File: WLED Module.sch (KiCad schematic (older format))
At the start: 16 parts, among them IC1 SN74AHCT125D, J1 Conn_01x06_Male, J2 1725669, J3 POWER_JACKPTH_BREAD, Q1 SS8050-G, Q2 SS8050-G, U1 ESP32-WROOM-32D, U2 AMS1117-3.3

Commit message: Various revisions:
Input lines on IC1 tied to VCC.
Input power connector changed to JST VH type.
Decoupling capacitors changed to 0.1uf.

Initial Gerber & other fab files generated.
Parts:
- removed J3: POWER_JACKPTH_BREAD, Connectors:POWER_JACK_PTH_BREAD, symbol SparkFun-Connectors:POWER_JACKPTH_BREAD
- added C6: 0.1uF 50V, Capacitor_SMD:C_0805_2012Metric_Pad1.15x1.40mm_HandSolder, symbol Device:C
- added F1: 10A, Fuse:Fuseholder_Blade_Mini_Keystone_3568, symbol Device:Fuse
- added H1, H2, H3, H4: MountingHole_Pad, MountingHole:MountingHole_3.2mm_M3_DIN965_Pad, symbol Mechanical:MountingHole_Pad
- added J3: Conn_01x02_Male, Connector_JST:JST_VH_B2PS-VH_1x02_P3.96mm_Horizontal, symbol Connector:Conn_01x02_Male
- added J4: Conn_01x02_Male, Connector_PinHeader_2.54mm:PinHeader_1x02_P2.54mm_Vertical, symbol Connector:Conn_01x02_Male
- added JP1: SolderJumper_2_Open, Jumper:SolderJumper-2_P1.3mm_Open_RoundedPad1.0x1.5mm, symbol Jumper:SolderJumper_2_Open
- added R4: 10K, Resistor_SMD:R_0805_2012Metric_Pad1.15x1.40mm_HandSolder, symbol Device:R
- C2, C3: footprint Capacitor_SMD:C_0603_1608Metric_Pad1.05x0.95mm_HandSolder -> Capacitor_SMD:C_0805_2012Metric_Pad1.15x1.40mm_HandSolder; LCSC (none) -> C45783
- C4: value 10uF -> 0.1uF; footprint Capacitor_SMD:C_0603_1608Metric_Pad1.05x0.95mm_HandSolder -> Capacitor_SMD:C_0805_2012Metric_Pad1.15x1.40mm_HandSolder; LCSC (none) -> C49678
- C5: value 10uf -> 0.1uF; footprint Capacitor_SMD:C_0603_1608Metric_Pad1.05x0.95mm_HandSolder -> Capacitor_SMD:C_0805_2012Metric_Pad1.15x1.40mm_HandSolder; LCSC (none) -> C15850
- IC1: LCSC (none) -> C155176
- J2: value 1725669 -> JST SM Connector; footprint SamacSys_Parts:1725669 -> Connector_PinHeader_2.54mm:PinHeader_1x03_P2.54mm_Vertical; symbol SamacSys_Parts:1725669 -> Connector:Conn_01x03_Male; Arrow Part Number 1725669 -> (none); Arrow Price/Stock https://www.arrow.com/en/products/1725669/phoenix-contact -> (none); Description 3 way PCB vertical mount terminal,2.54mm 3 way PCB vertical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 -> (none); Height 8.5 -> (none); Manufacturer_Name Phoenix Contact -> (none); Manufacturer_Part_Number 1725669 -> (none); Mouser Part Number 651-1725669 -> (none); Mouser Price/Stock https://www.mouser.co.uk/ProductDetail/Phoenix-Contact/1725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 -> (none)
- Q1, Q2: value SS8050-G -> SS8050; footprint SamacSys_Parts:SOT95P240X115-3N -> Package_TO_SOT_SMD:SOT-323_SC-70_Handsoldering; Arrow Part Number SS8050-G -> (none); Arrow Price/Stock https://www.arrow.com/en/products/ss8050-g/comchip-technolo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 -> (none); Description Bipolar Transistors - BJT NPN TRANSISTOR 1.5A 40V -> (none); Height 1.15 -> (none); LCSC (none) -> C109068; Manufacturer_Name Comchip Technology -> (none); Manufacturer_Part_Number SS8050-G -> (none); Mouser Part Number 750-SS8050-G -> (none); Mouser Price/Stock https://www.mouser.co.uk/ProductDetail/Comchip-Technology/S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 -> (none)
- R1, R2: footprint Resistor_SMD:R_0603_1608Metric_Pad1.05x0.95mm_HandSolder -> Resistor_SMD:R_0805_2012Metric_Pad1.15x1.40mm_HandSolder; symbol SparkFun-Resistors:RESISTOR0402 -> Device:R; Field4 (none) -> (none); LCSC (none) -> C17414
- R3: value 470 -> 470R; LCSC (none) -> C17710
- U2: LCSC (none) -> C6186
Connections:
- net +3V3: now also R4.1
- net +5V: now also IC1.2 (1A), IC1.5 (2A), IC1.9 (3A), J2.3 (Pin_3), F1.1, J4.1 (Pin_1); no longer J2.1
- net DTR: now also J1.3 (Pin_3); no longer J1.2 (Pin_2)
- net EN: now also C6.1, R4.2
- net GND: now also J2.1 (Pin_1), C6.2, H1.1, H2.1, H3.1, H4.1, J3.2 (Pin_2), J4.2 (Pin_2); no longer J2.3
- net GPIO2: now also JP1.1 (A)
- net RTS: now also J1.2 (Pin_2), R1.2; no longer J1.3 (Pin_3), R1.1
- net RX: now also J1.4 (Pin_4); no longer J1.5 (Pin_5)
- net TX: now also J1.5 (Pin_5); no longer J1.4 (Pin_4)
- net at Q1.1: now also R1.1; no longer R1.2
- net at IC1.11 (4Y), R3.2: now also JP1.2 (B)
- new net: F1.2, J3.1 (Pin_1)
- no-connect marks 37 -> 34
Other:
- note added: "Mounting holes"

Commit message: V1.2
* Auto-save circuitry replaced in favour of ESP-Prog interface.
* Ancillary components rearranged.
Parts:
- removed J1: Conn_01x06_Male, Connector_PinHeader_2.54mm:PinHeader_1x06_P2.54mm_Vertical, symbol Connector:Conn_01x06_Male
- removed Q1, Q2: SS8050, Package_TO_SOT_SMD:SOT-323_SC-70_Handsoldering, symbol SamacSys_Parts:SS8050-G
- removed R1, R2: 10k, Resistor_SMD:R_0805_2012Metric_Pad1.15x1.40mm_HandSolder, symbol Device:R
- added J1: Conn_02x03_Odd_Even, Connector_IDC:IDC-Header_2x03_P2.54mm_Vertical, symbol Connector_Generic:Conn_02x03_Odd_Even
- C1: footprint SamacSys_Parts:CAPPRD350W65D800H1300 -> SamacSys:CAPPRD350W65D800H1300; symbol SamacSys_Parts:EEU-FR0J102 -> WLED-Module-rescue:EEU-FR0J102-SamacSys_Parts
- IC1: footprint SamacSys_Parts:SOIC127P600X175-14N -> SamacSys:SOIC127P600X175-14N; symbol SamacSys_Parts:SN74AHCT125D -> WLED-Module-rescue:SN74AHCT125D-SamacSys_Parts
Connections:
- net +3V3: now also J1.2 (Pin_2)
- net +5V: now also IC1.12 (4A); no longer IC1.5 (2A)
- net DAT: now also R3.2; no longer R3.1
- net EN: now also J1.1 (Pin_1)
- net GND: now also IC1.4 (2~OE), J1.4 (Pin_4); no longer IC1.13 (4~OE)
- net GPIO0: now also J1.6 (Pin_6)
- net RX: now also J1.5 (Pin_5)
- net TX: now also J1.3 (Pin_3)
- net GPIO16: now reaches U1.27 (IO16)
- net GPIO16: now also IC1.5 (2A), JP1.2 (B)
- net at IC1.6 (2Y): now also JP1.1 (A), R3.1
- removed net GPIO2: IC1.12 (4A), JP1.1 (A), U1.24 (IO2)
- now unconnected: IC1.11 (4Y)
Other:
- note removed: "Auto-Reset Circuit"
- note removed: "Programming Header"
- moved on the sheet: JP1, R3

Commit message: Add the rest of the files. Duh.
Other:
- note added: "ESP-Prog Programming Interface"
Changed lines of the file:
@@
 encoding utf-8
 Sheet 1 1
-Title ""
+Title "WLED Module"
 Date ""
-Rev ""
-Comp ""
+Rev "v1.2"
+Comp "marknotgeorge"
 Comment1 ""
 Comment2 ""
@@
 	1050 6700 1200 6700
 NoConn ~ 2500 6600
+Text Notes 3200 2000 0    50   ~ 0
+ESP-Prog Programming Interface
 $EndSCHEMATC

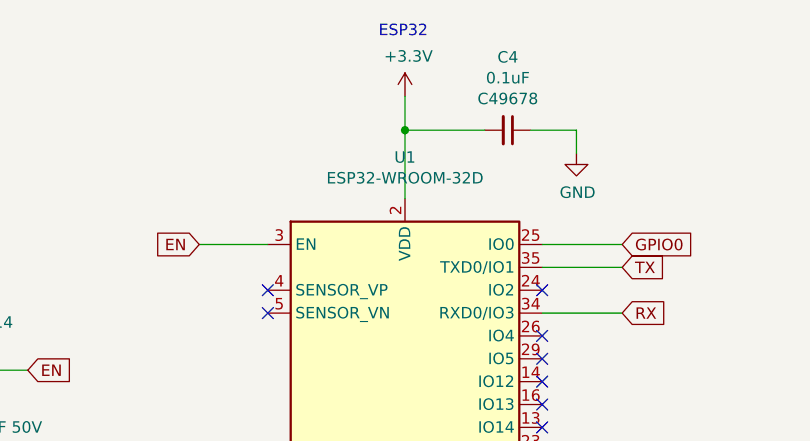
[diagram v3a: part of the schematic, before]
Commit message: Adjustments for JLCPCB assembly.
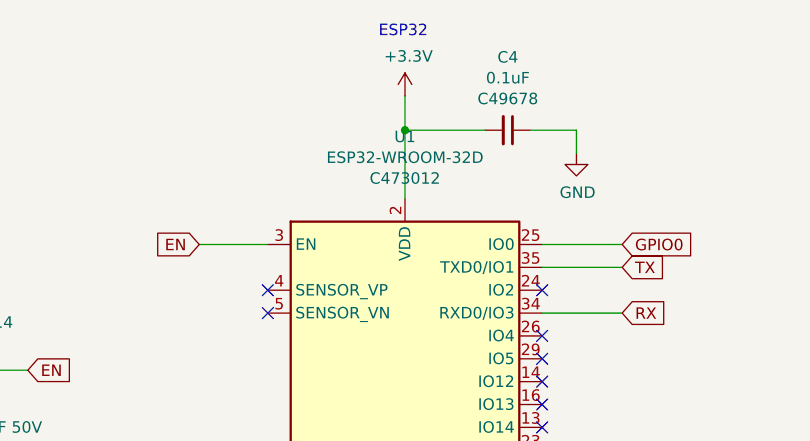
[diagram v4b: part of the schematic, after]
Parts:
- U1: LCSC (none) -> C473012
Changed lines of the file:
@@
 U 1 1 5FA1923B
 P 8350 2800
-F 0 "U1" H 8350 4381 50  0000 C CNN
-F 1 "ESP32-WROOM-32D" H 8350 4290 50  0000 C CNN
+F 0 "U1" H 8350 4471 50  0000 C CNN
+F 1 "ESP32-WROOM-32D" H 8350 4380 50  0000 C CNN
 F 2 "RF_Module:ESP32-WROOM-32" H 8350 1300 50  0001 C CNN
 F 3 "https://www.espressif.com/sites/default/files/documentation/esp32-wroom-32d_esp32-wroom-32u_datasheet_en.pdf" H 8050 2850 50  0001 C CNN
+F 4 "C473012" H 8350 4289 50  0000 C CNN "LCSC"
 	1    8350 2800
 	1    0    0    -1
